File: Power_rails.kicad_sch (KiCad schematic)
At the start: 74 parts

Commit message: SDRAM, bank5
last iteration of sdram. max optimization routing and space wise. Traced 2 frams to Bank 5. Fanout of bank 5 for DF9
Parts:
- L5: footprint Inductor_SMD:L_0805_2012Metric_Pad1.05x1.20mm_HandSolder -> Inductor_SMD:L_0402_1005Metric_Pad0.77x0.64mm_HandSolder
- R21, R22, R23, R24, R25, R26, R28, R29, R30: footprint (none) -> Resistor_SMD:R_0402_1005Metric_Pad0.72x0.64mm_HandSolder
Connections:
- net VDDIO_0 renamed VDDIO_8
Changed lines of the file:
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@@
 			)
 		)
-		(property "Footprint" ""
+		(property "Footprint" "Resistor_SMD:R_0402_1005Metric_Pad0.72x0.64mm_HandSolder"
 			(at 30.48 29.21 0)
 			(effects
@@
 			)
 		)
-		(property "Footprint" ""
+		(property "Footprint" "Resistor_SMD:R_0402_1005Metric_Pad0.72x0.64mm_HandSolder"
 			(at 223.52 99.06 0)
 			(effects
@@
 			)
 		)
-		(property "Footprint" ""
+		(property "Footprint" "Resistor_SMD:R_0402_1005Metric_Pad0.72x0.64mm_HandSolder"
 			(at 153.67 139.7 0)
 			(effects
@@
 	)
 	(symbol
+		(lib_id "DataHub_PWR_symbols:VDDIO_8")
+		(at 231.14 97.79 0)
+		(unit 1)
+		(exclude_from_sim no)
+		(in_bom yes)
+		(on_board yes)
+		(dnp no)
+		(fields_autoplaced yes)
+		(property "Reference" "#PWR081"
+			(at 215.138 92.71 0)
+			(effects
+				(font
+					(size 1.27 1.27)
+				)
+				(hide yes)
+			)
+		)
+		(property "Value" "VDDIO_8"
+			(at 231.14 92.71 0)
+			(effects
+				(font
+					(size 1.27 1.27)
+				)
+			)
+		)
+		(property "Footprint" ""
+			(at 231.14 97.79 0)
+			(effects
+				(font
+					(size 1.27 1.27)
+				)
+				(hide yes)
+			)
+		)
+		(property "Datasheet" ""
+			(at 231.14 97.79 0)
+			(effects
+				(font
+					(size 1.27 1.27)
+				)
+				(hide yes)
+			)
+		)
+		(property "Description" "Power symbol creates a global label with name \"VDDIO_8\""
+			(at 229.108 88.392 0)
+			(effects
+				(font
+					(size 1.27 1.27)
+				)
+				(hide yes)
+			)
+		)
+		(pin "1"
+		)
+		(instances
+			(project ""
+				(path "/ae14ff2f-b8e3-4dd1-9329-e73906805e39/7c344aa7-1e72-4ff4-b2c4-18ee529166e7"
+					(reference "#PWR081")
+					(unit 1)
+				)
+			)
+		)
+	)
+	(symbol
 		(lib_name "C_Small_1")
 		(lib_id "Device:C_Small")
@@
 			)
 		)
-		(property "Footprint" ""
+		(property "Footprint" "Resistor_SMD:R_0402_1005Metric_Pad0.72x0.64mm_HandSolder"
 			(at 153.67 119.38 0)
 			(effects
@@
 			)
 		)
-		(property "Footprint" ""
+		(property "Footprint" "Resistor_SMD:R_0402_1005Metric_Pad0.72x0.64mm_HandSolder"
 			(at 223.52 119.38 0)
 			(effects
@@
 			)
 		)
-		(property "Footprint" ""
+		(property "Footprint" "Resistor_SMD:R_0402_1005Metric_Pad0.72x0.64mm_HandSolder"
 			(at 60.96 29.21 0)
 			(effects
@@
 			)
 		)
-		(property "Footprint" ""
+		(property "Footprint" "Resistor_SMD:R_0402_1005Metric_Pad0.72x0.64mm_HandSolder"
 			(at 90.17 29.21 0)
 			(effects
@@
 			)
 		)
-		(property "Footprint" ""
+		(property "Footprint" "Resistor_SMD:R_0402_1005Metric_Pad0.72x0.64mm_HandSolder"
 			(at 181.61 76.2 0)
 			(effects
@@
 			)
 		)
-		(property "Footprint" ""
+		(property "Footprint" "Resistor_SMD:R_0402_1005Metric_Pad0.72x0.64mm_HandSolder"
 			(at 223.52 139.7 0)
 			(effects
@@
 			)
 		)
-		(property "Footprint" "Inductor_SMD:L_0805_2012Metric_Pad1.05x1.20mm_HandSolder"
+		(property "Footprint" "Inductor_SMD:L_0402_1005Metric_Pad0.77x0.64mm_HandSolder"
 			(at 248.92 76.2 0)
 			(effects
@@
 					(unit 1)
 				)
-			)
-		)
-	)
-	(symbol
-		(lib_id "DataHub_PWR_symbols:VDDIO_0")
-		(at 231.14 97.79 0)
-		(unit 1)
-		(exclude_from_sim no)
-		(in_bom yes)
-		(on_board yes)
-		(dnp no)
-		(fields_autoplaced yes)
-		(property "Reference" "#PWR087"
-			(at 215.138 92.71 0)
-			(effects
-				(font
-					(size 1.27 1.27)
-				)
-				(hide yes)
-			)
-		)
-		(property "Value" "VDDIO_0"
-			(at 231.14 92.71 0)
-			(effects
-				(font
-					(size 1.27 1.27)
-				)
-			)
-		)
-		(property "Footprint" ""
-			(at 231.14 97.79 0)
-			(effects
-				(font
-					(size 1.27 1.27)
-				)
-				(hide yes)
-			)
-		)
-		(property "Datasheet" ""
-			(at 231.14 97.79 0)
-			(effects
-				(font
-					(size 1.27 1.27)
-				)
-				(hide yes)
-			)
-		)
-		(property "Description" "Power symbol creates a global label with name \"VDDIO_0\""
-			(at 229.108 88.392 0)
-			(effects
-				(font
-					(size 1.27 1.27)
-				)
-				(hide yes)
-			)
-		)
-		(pin "1"
-		)
-		(instances
-			(project "PCB_Project"
-				(path "/ae14ff2f-b8e3-4dd1-9329-e73906805e39/7c344aa7-1e72-4ff4-b2c4-18ee529166e7"
-					(reference "#PWR087")
-					(unit 1)
-				)

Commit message: full components, LEDS, changed edges
all components on pcb editor. added and  routed leds and 2 PLL. changed edges o have more space
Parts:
- removed R21, R28, R29, R30: 0 Ohm, Resistor_SMD:R_0402_1005Metric_Pad0.72x0.64mm_HandSolder, symbol Device:R_Small
- added C45, C52, C53, C54, C55, C56, C57, C58, C61, C63, C81, C97: 10uF, Capacitor_SMD:C_0603_1608Metric_Pad1.08x0.95mm_HandSolder, symbol Device:C_Small
- added C59: --, Capacitor_SMD:C_0402_1005Metric_Pad0.74x0.62mm_HandSolder, symbol Device:C_Small
- added Q1, Q2: SOC2222AHRG, DataHub_Footprints:NPN_LCC-3_STM, symbol Simulation_SPICE:NPN
- added R34, R37, R41: 100k, Resistor_SMD:R_0402_1005Metric_Pad0.72x0.64mm_HandSolder, symbol Device:R_Small
- added R35, R42: 4k02, Resistor_SMD:R_0402_1005Metric_Pad0.72x0.64mm_HandSolder, symbol Device:R_Small
- added R36, R39, R43: 1k, Resistor_SMD:R_0402_1005Metric_Pad0.72x0.64mm_HandSolder, symbol Device:R_Small
- added R38: 1k4, Resistor_SMD:R_0402_1005Metric_Pad0.72x0.64mm_HandSolder, symbol Device:R_Small
- added R40: --, Resistor_SMD:R_0402_1005Metric_Pad0.72x0.64mm_HandSolder, symbol Device:R_Small
- added U10, U8, U9: MAX8556ETE, DataHub_Footprints:MAX8556, symbol MAX_LDO:MAX8556ETE
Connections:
- net +1V7_IN: now also C55.1, C56.1, U10.1 (IN), U10.2 (IN), U10.3 (IN), U10.4 (IN), U10.5 (IN), U10.6 (IN)
- net +3V3_IN: now also C61.1, C63.1, Q1.1 (C), Q2.1 (C), R41.1, U8.1 (IN), U8.2 (IN), U8.3 (IN), U8.4 (IN), U8.5 (IN), U8.6 (IN)
- net GND: now also C45.2, C52.2, C53.2, C54.2, C55.2, C56.2, C57.2, C58.2, C59.2, C61.2, C63.2, C81.2, C97.2, R36.2, R39.2, R43.2, U10.14 (GND), U10.15 (NC), U10.17 (EPAD), U8.14 (GND), U8.15 (NC), U8.17 (EPAD), U9.14 (GND), U9.15 (NC), U9.17 (EPAD)
- net VDD1V2: now also C57.1, C58.1, R38.1, U10.10 (OUT), U10.11 (OUT), U10.7 (OUT), U10.8 (OUT), U10.9 (OUT)
- net VDD2V5: now also C53.1, C54.1, C81.1, C97.1, R35.1, R42.1, U8.10 (OUT), U8.11 (OUT), U8.7 (OUT), U8.8 (OUT), U8.9 (OUT), U9.10 (OUT), U9.11 (OUT), U9.7 (OUT), U9.8 (OUT), U9.9 (OUT)
- net VDD3V3: now also Q1.3 (E), Q2.3 (E), R40.1, U8.16 (EN)
- net VDDIO_8 renamed VDDIO_0
- new net: C59.1, Q2.2 (B), R40.2
- new net: R34.2, U10.16 (EN), U9.12 (POK(POR))
- new net: R35.2, R36.1, U9.13 (FB)
- new net: R42.2, R43.1, U8.13 (FB)
- new net: Q1.2 (B), R37.2, U10.12 (POK(POR))
- new net: R38.2, R39.1, U10.13 (FB)
- new net: R41.2, U8.12 (POK(POR))
- new net +3V_IN: C45.1, C52.1, R34.1, R37.1, U9.1 (IN), U9.16 (EN), U9.2 (IN), U9.3 (IN), U9.4 (IN), U9.5 (IN), U9.6 (IN)
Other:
- moved on the sheet: C79, C80, C82, C83, C88, C89, C90, R23, R25

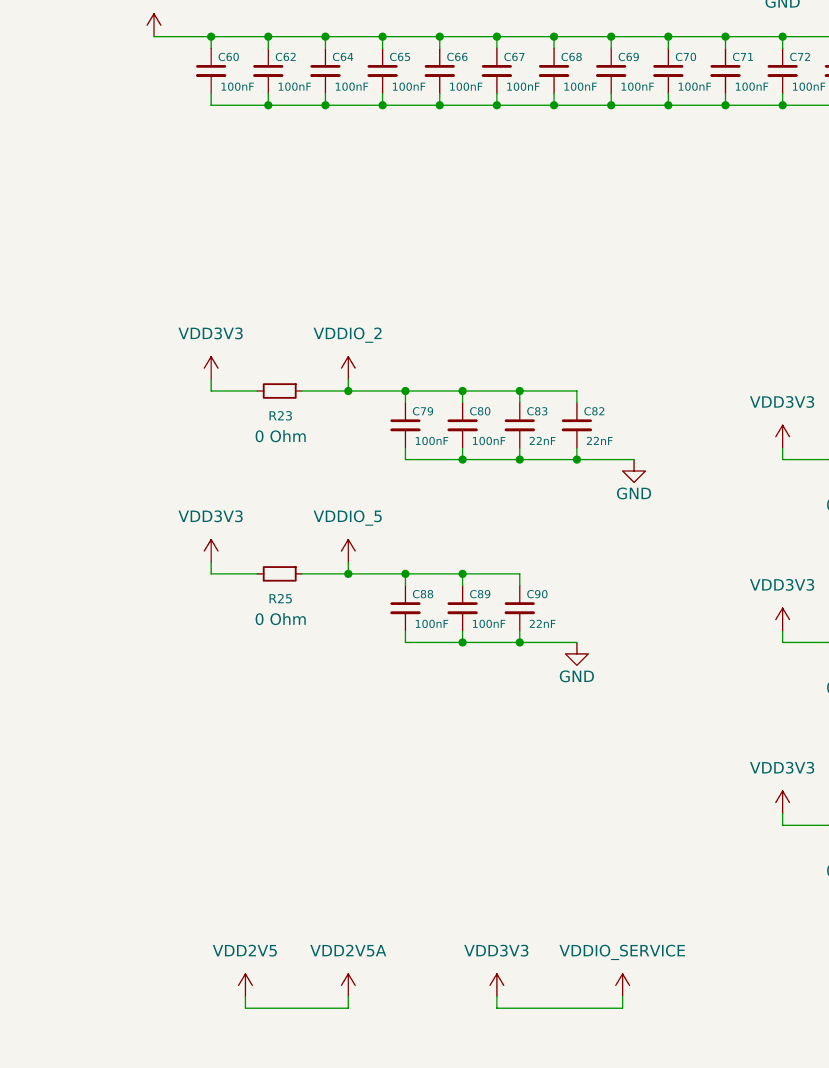
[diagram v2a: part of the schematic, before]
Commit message: SPW Bank0
completed SPW, rotated edges and adjusted dimensions to make the extra sdram bga fit. completed Bank 0 (still to route to connector). Started fanout of bga sdram
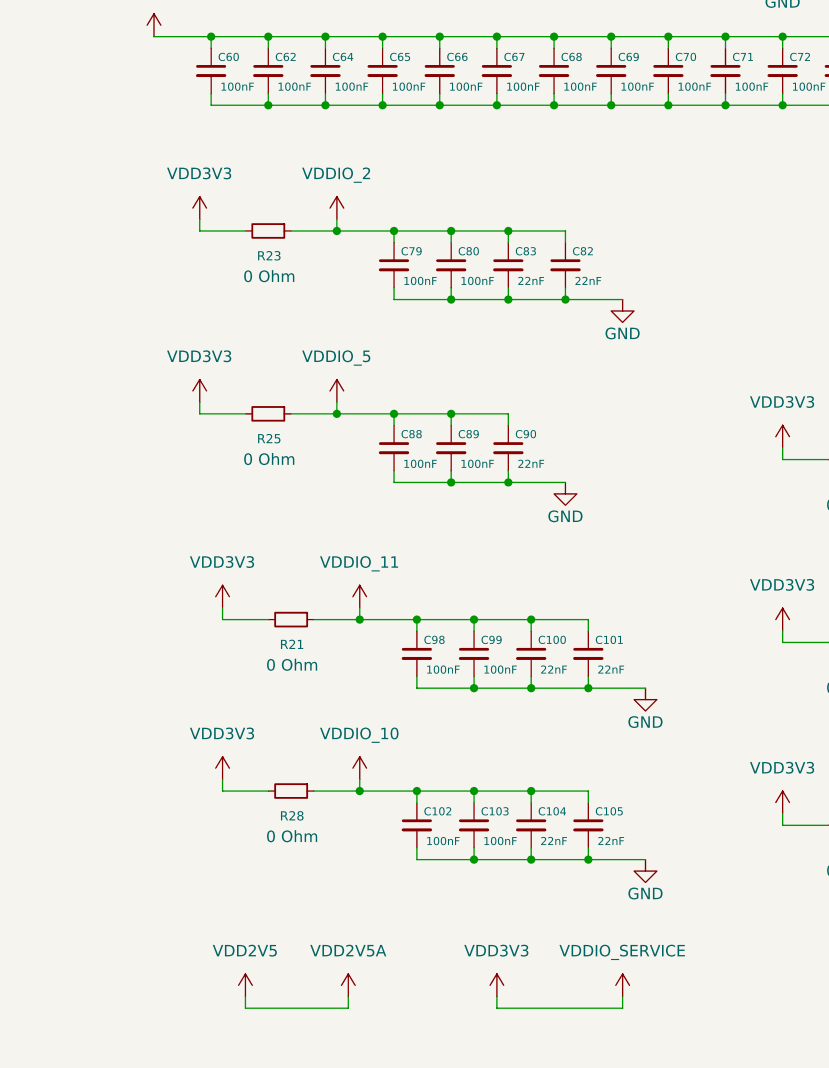
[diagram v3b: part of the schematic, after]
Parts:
- added C100, C101, C104, C105: 22nF, Capacitor_SMD:C_0402_1005Metric_Pad0.74x0.62mm_HandSolder, symbol Device:C_Small
- added C102, C103, C98, C99: 100nF, Capacitor_SMD:C_0402_1005Metric_Pad0.74x0.62mm_HandSolder, symbol Device:C_Small
- added R21, R28: 0 Ohm, Resistor_SMD:R_0402_1005Metric_Pad0.72x0.64mm_HandSolder, symbol Device:R_Small
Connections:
- net GND: now also C100.2, C101.2, C102.2, C103.2, C104.2, C105.2, C98.2, C99.2
- net VDD3V3: now also R21.2, R28.2
- new net VDDIO_10: C102.1, C103.1, C104.1, C105.1, R28.1
- new net VDDIO_11: C100.1, C101.1, C98.1, C99.1, R21.1
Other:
- moved on the sheet: C79, C80, C82, C83, C88, C89, C90, R23, R25

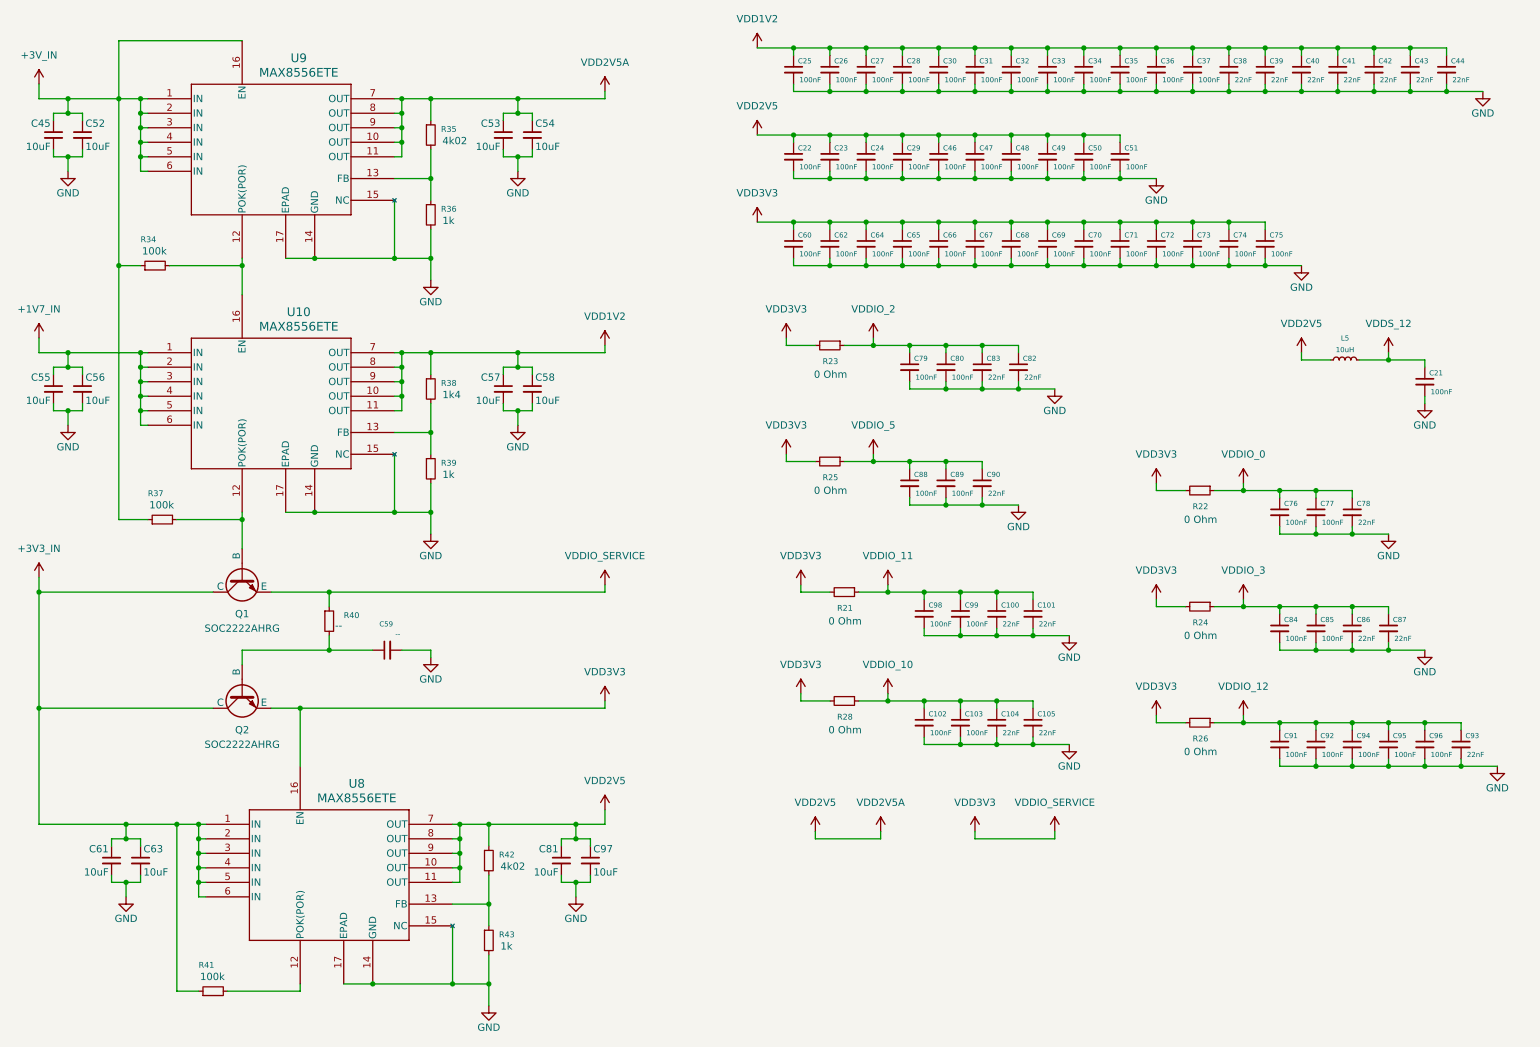
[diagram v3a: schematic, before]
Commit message: CFG, bga sdram, banks to connectors, docoupling
Finished completely routing bga sdram, finished tracing Banks to connectors DF9. Finished tracing Picoblade, diode, reset supervisor. Finished tracing LEDS on bank 5. Finished decoupling all banks and core. Missing only the power tree and power rail level decoupling.
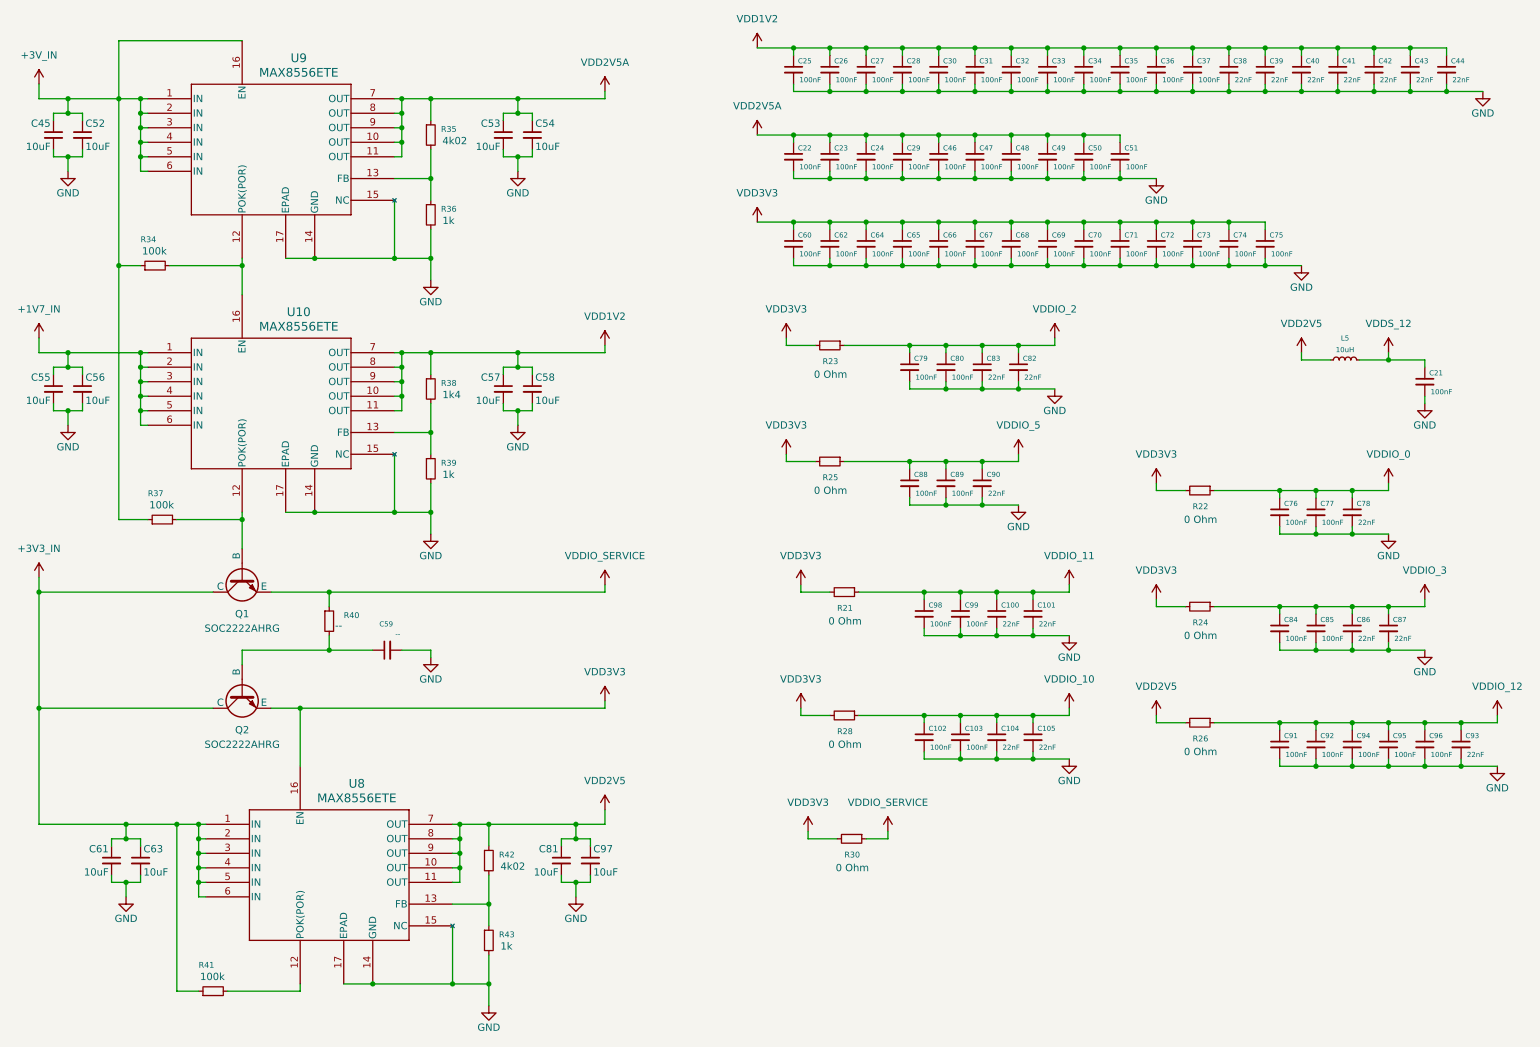
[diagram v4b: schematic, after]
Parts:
- added R30: 0 Ohm, Resistor_SMD:R_0402_1005Metric_Pad0.72x0.64mm_HandSolder, symbol Device:R_Small
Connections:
- net VDD2V5: now also R26.2; no longer C22.1, C23.1, C24.1, C29.1, C46.1, C47.1, C48.1, C49.1, C50.1, C51.1, C53.1, C54.1, R35.1, U9.10 (OUT), U9.11 (OUT), U9.7 (OUT), U9.8 (OUT), U9.9 (OUT)
- net VDD3V3: now also R30.2; no longer Q1.3 (E), R26.2, R40.1
- new net VDD2V5A: C22.1, C23.1, C24.1, C29.1, C46.1, C47.1, C48.1, C49.1, C50.1, C51.1, C53.1, C54.1, R35.1, U9.10 (OUT), U9.11 (OUT), U9.7 (OUT), U9.8 (OUT), U9.9 (OUT)
- new net VDDIO_SERVICE: Q1.3 (E), R30.1, R40.1
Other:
- moved on the sheet: C102, C103, C104, C105, R28

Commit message: power tree
power tree defined. Few changes remaining but almost finalized
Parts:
- removed C45, C52, C53, C54, C55, C56, C57, C58, C61, C63, C81, C97: 10uF, Capacitor_SMD:C_0603_1608Metric_Pad1.08x0.95mm_HandSolder, symbol Device:C_Small
- removed C59: --, Capacitor_SMD:C_0402_1005Metric_Pad0.74x0.62mm_HandSolder, symbol Device:C_Small
- removed Q1, Q2: SOC2222AHRG, DataHub_Footprints:NPN_LCC-3_STM, symbol Simulation_SPICE:NPN
- removed R21, R22, R23, R24, R25, R28: 0 Ohm, Resistor_SMD:R_0402_1005Metric_Pad0.72x0.64mm_HandSolder, symbol Device:R_Small
- removed R34, R37, R41: 100k, Resistor_SMD:R_0402_1005Metric_Pad0.72x0.64mm_HandSolder, symbol Device:R_Small
- removed R35, R42: 4k02, Resistor_SMD:R_0402_1005Metric_Pad0.72x0.64mm_HandSolder, symbol Device:R_Small
- removed R36, R39, R43: 1k, Resistor_SMD:R_0402_1005Metric_Pad0.72x0.64mm_HandSolder, symbol Device:R_Small
- removed R38: 1k4, Resistor_SMD:R_0402_1005Metric_Pad0.72x0.64mm_HandSolder, symbol Device:R_Small
- removed R40: --, Resistor_SMD:R_0402_1005Metric_Pad0.72x0.64mm_HandSolder, symbol Device:R_Small
- removed U10, U8, U9: MAX8556ETE, DataHub_Footprints:MAX8556, symbol MAX_LDO:MAX8556ETE
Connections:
- net VDDIO_0 is gone; now on net VDD3V3: C76.1, C77.1, C78.1
- net VDDIO_10 is gone; now on net VDD3V3: C102.1, C103.1, C104.1, C105.1
- net VDDIO_11 is gone; now on net VDD3V3: C100.1, C101.1, C98.1, C99.1
- net VDDIO_2 is gone; now on net VDD3V3: C79.1, C80.1, C82.1, C83.1
- net VDDIO_3 is gone; now on net VDD3V3: C84.1, C85.1, C86.1, C87.1
- net VDDIO_5 is gone; now on net VDD3V3: C88.1, C89.1, C90.1
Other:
- moved on the sheet: C100, C101, C102, C103, C104, C105, C21, C22, C23, C24, C25, C26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

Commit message: finished PCB
finished power tree and power planes. Completed silkscreen placement. Added test points
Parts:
- removed R26, R30: 0 Ohm, Resistor_SMD:R_0402_1005Metric_Pad0.72x0.64mm_HandSolder, symbol Device:R_Small
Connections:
- net VDDIO_12 is gone; now on net VDD2V5: C91.1, C92.1, C93.1, C94.1, C95.1, C96.1
